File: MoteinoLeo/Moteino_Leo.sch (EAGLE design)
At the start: 21 parts, among them IC3 MCP1703CB, U3 ATMEGA32U4, X1 16Mhz

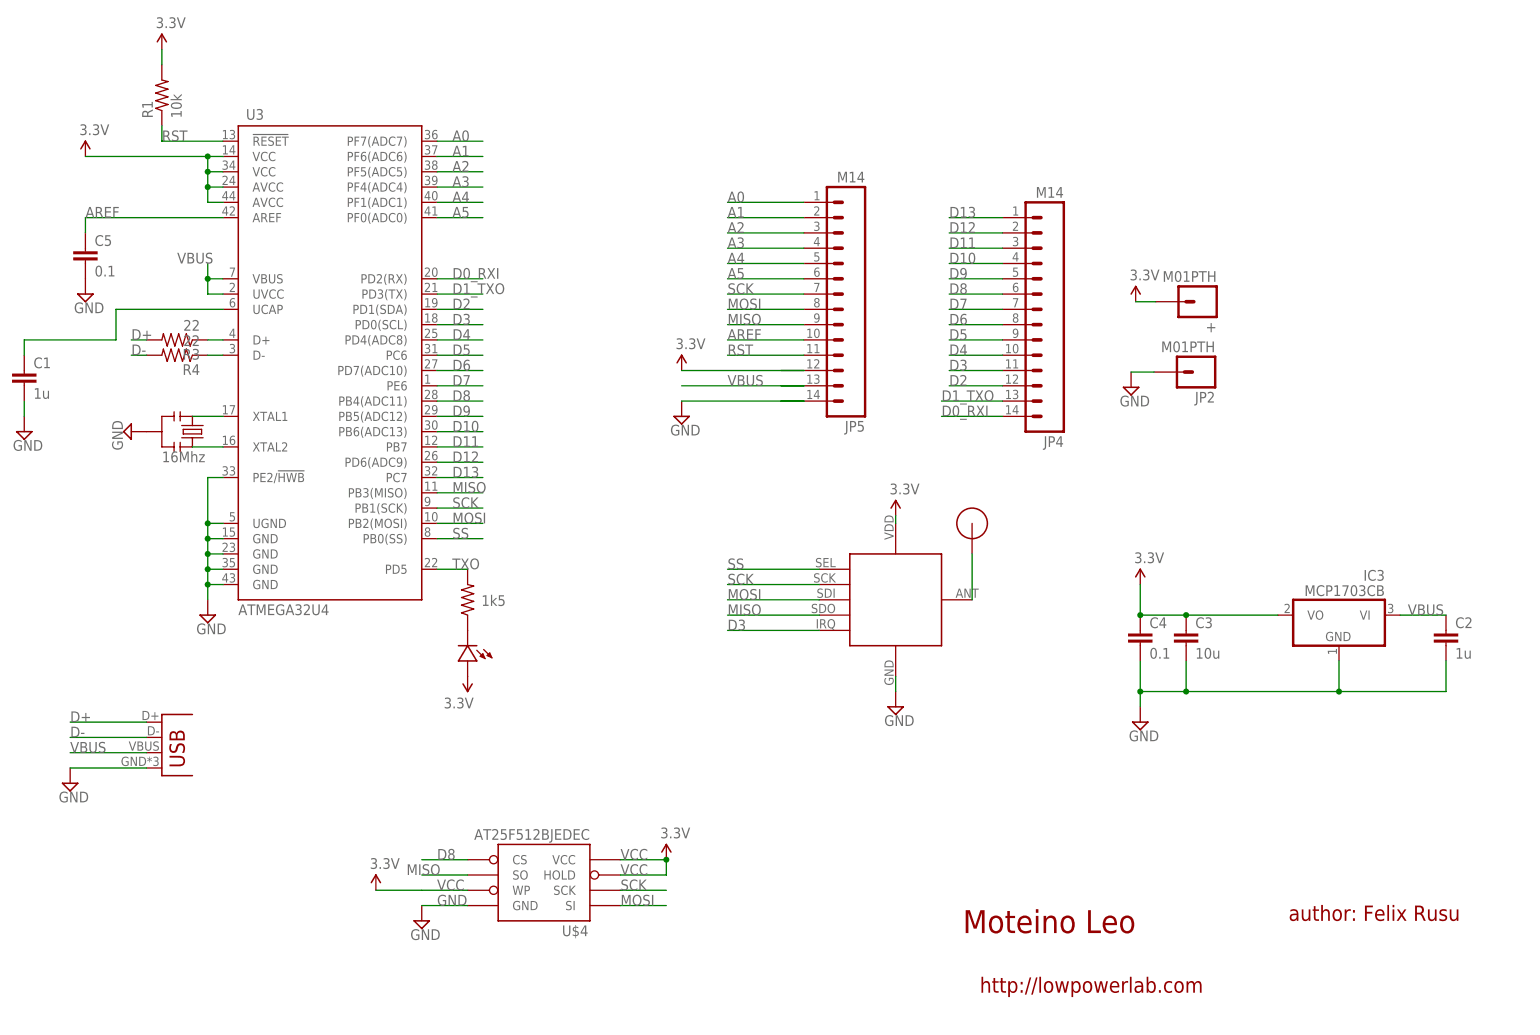
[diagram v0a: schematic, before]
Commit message: Update to R1 production schematic
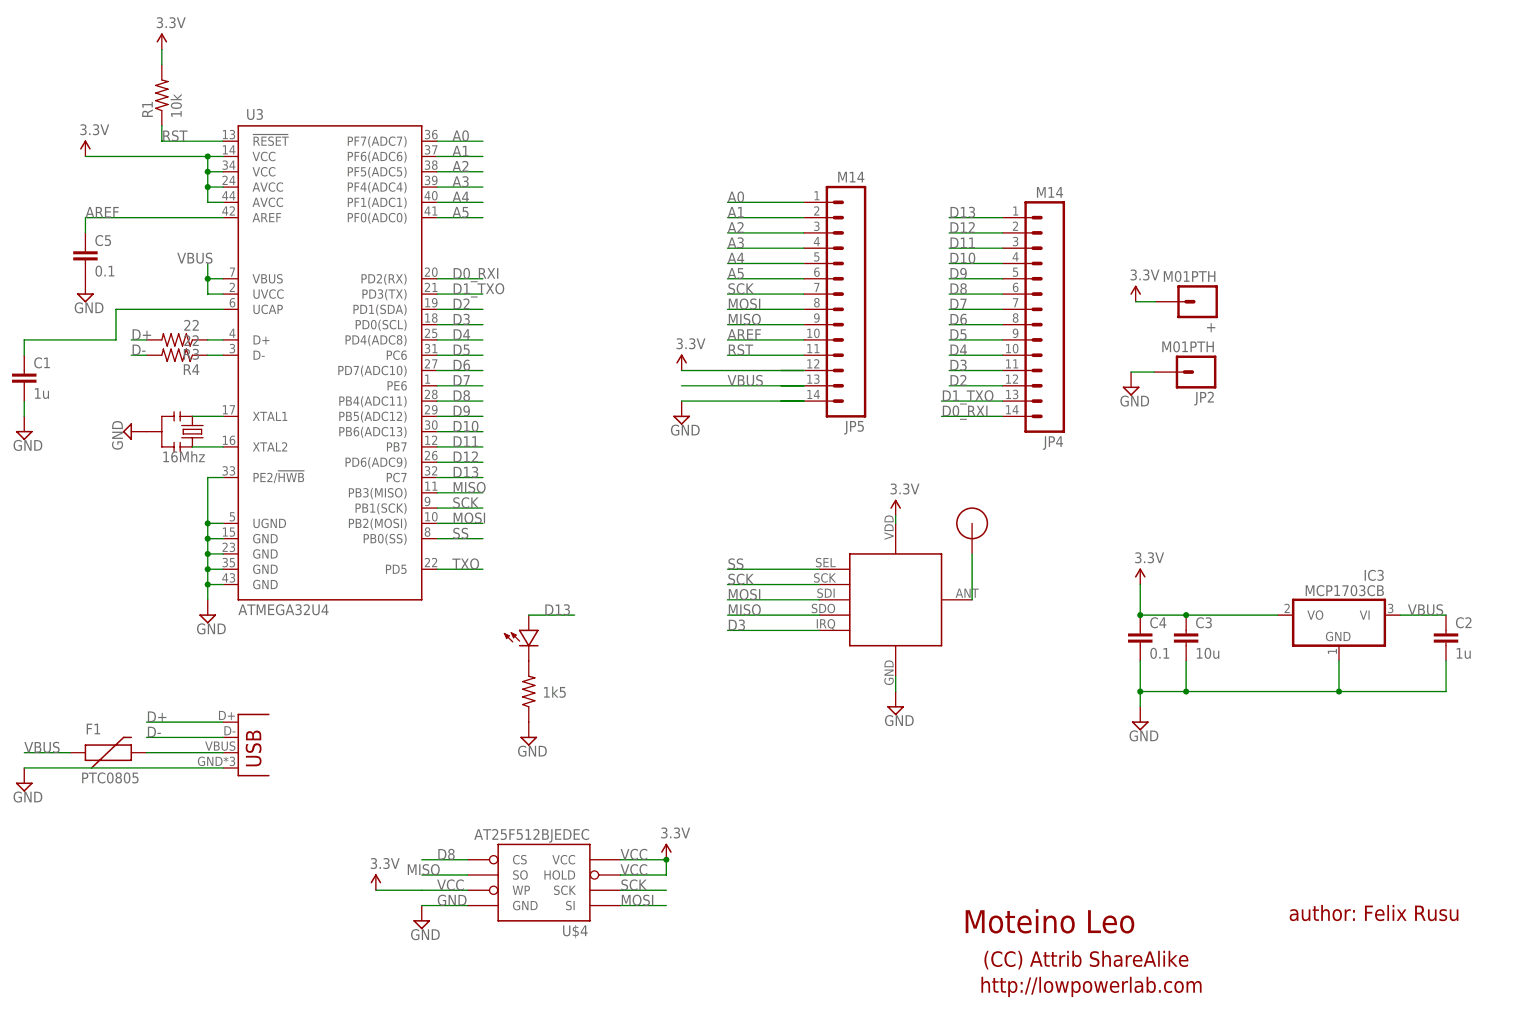
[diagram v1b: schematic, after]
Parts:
- added F1: PTC0805, LowPowerLab:PTC0805
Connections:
- new net USBPOWER: F1.2, JP3.VBUS
- net D13: now also U$2.PLUS
- net GND: now also R2.1
- net N$1: now also R2.2; no longer R2.1
- net TXO: no longer R2.2
- net VBUS: now also F1.1; no longer JP3.VBUS
- net VCC: no longer U$2.PLUS
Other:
- note added: "(CC) Attrib ShareAlike"
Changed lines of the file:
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@@
 <part name="R3" library="LowPowerLab" deviceset="RESISTOR" device="0603-RES" value="22"/>
 <part name="R4" library="LowPowerLab" deviceset="RESISTOR" device="0603-RES" value="22"/>
-<part name="P+6" library="SparkFun" deviceset="VCC" device="" value="3.3V"/>
+<part name="SUPPLY6" library="supply2" deviceset="GND" device=""/>
+<part name="F1" library="LowPowerLab" deviceset="PTC" device="0805"/>
 </parts>
 <sheets>
@@
 <text x="217.678" y="20.32" size="2.54" layer="94" font="vector">author: Felix Rusu</text>
 <text x="166.37" y="8.382" size="2.54" layer="94" font="vector">http://lowpowerlab.com</text>
+<text x="166.878" y="12.7" size="2.54" layer="94" font="vector">(CC) Attrib ShareAlike</text>
 </plain>
 <instances>
@@
 <instance part="C2" gate="G$1" x="243.84" y="66.04"/>
 <instance part="C3" gate="G$1" x="200.66" y="66.04"/>
-<instance part="U$2" gate="G$1" x="81.28" y="66.04" smashed="yes" rot="R270"/>
-<instance part="R2" gate="G$1" x="81.28" y="73.66" smashed="yes" rot="R90">
-<attribute name="VALUE" x="87.63" y="74.422" size="1.778" layer="96" rot="R180"/>
+<instance part="U$2" gate="G$1" x="91.44" y="66.04" smashed="yes" rot="R90"/>
+<instance part="R2" gate="G$1" x="91.44" y="58.42" smashed="yes" rot="R90">
+<attribute name="VALUE" x="97.79" y="59.182" size="1.778" layer="96" rot="R180"/>
 </instance>
 <instance part="RFM12B" gate="G$1" x="152.4" y="73.66" smashed="yes"/>
@@
 <instance part="SUPPLY5" gate="GND" x="7.62" y="101.6"/>
 <instance part="SUPPLY12" gate="GND" x="17.78" y="124.46"/>
-<instance part="JP3" gate="G$1" x="30.48" y="45.72"/>
-<instance part="SUPPLY13" gate="GND" x="15.24" y="43.18"/>
+<instance part="JP3" gate="G$1" x="43.18" y="45.72"/>
+<instance part="SUPPLY13" gate="GND" x="7.62" y="43.18"/>
 <instance part="JP4" gate="G$1" x="180.34" y="119.38" rot="R180"/>
 <instance part="JP5" gate="G$1" x="147.32" y="121.92" rot="R180"/>
 <instance part="R3" gate="G$1" x="33.02" y="116.84" rot="R180"/>
 <instance part="R4" gate="G$1" x="33.02" y="114.3" rot="R180"/>
-<instance part="P+6" gate="1" x="81.28" y="60.96" rot="R180"/>
+<instance part="SUPPLY6" gate="GND" x="91.44" y="50.8"/>
+<instance part="F1" gate="G$1" x="20.32" y="48.26"/>
 </instances>
 <busses>
@@
 <segment>
 <pinref part="JP3" gate="G$1" pin="GND"/>
-<wire x1="27.94" y1="45.72" x2="15.24" y2="45.72" width="0.1524" layer="91"/>
+<wire x1="40.64" y1="45.72" x2="7.62" y2="45.72" width="0.1524" layer="91"/>
 <pinref part="SUPPLY13" gate="GND" pin="GND"/>
+</segment>
+<segment>
+<pinref part="R2" gate="G$1" pin="1"/>
+<pinref part="SUPPLY6" gate="GND" pin="GND"/>
 </segment>
 </net>
@@
 <pinref part="SUPPLY11" gate="1" pin="VCC"/>
 </segment>
-<segment>
-<pinref part="P+6" gate="1" pin="VCC"/>
-<pinref part="U$2" gate="G$1" pin="PLUS"/>
-</segment>
 </net>
 <net name="D9" class="0">
@@
 </segment>
 <segment>
-<pinref part="JP3" gate="G$1" pin="VBUS"/>
-<wire x1="27.94" y1="48.26" x2="15.24" y2="48.26" width="0.1524" layer="91"/>
-<label x="15.24" y="48.26" size="1.778" layer="95"/>
-</segment>
-<segment>
 <wire x1="133.35" y1="109.22" x2="137.16" y2="109.22" width="0.1524" layer="91"/>
 <label x="124.46" y="109.22" size="1.778" layer="95"/>
@@
 <wire x1="137.16" y1="109.22" x2="116.84" y2="109.22" width="0.1524" layer="91"/>
 </segment>
+<segment>
+<pinref part="F1" gate="G$1" pin="1"/>
+<wire x1="15.24" y1="48.26" x2="7.62" y2="48.26" width="0.1524" layer="91"/>
+<label x="7.62" y="48.26" size="1.778" layer="95"/>
+</segment>
 </net>
 <net name="D+" class="0">
@@
 <segment>
 <pinref part="JP3" gate="G$1" pin="D+"/>
-<wire x1="27.94" y1="53.34" x2="15.24" y2="53.34" width="0.1524" layer="91"/>
-<label x="15.24" y="53.34" size="1.778" layer="95"/>
+<wire x1="40.64" y1="53.34" x2="27.94" y2="53.34" width="0.1524" layer="91"/>
+<label x="27.94" y="53.34" size="1.778" layer="95"/>
 </segment>
 </net>
@@
 <segment>
 <pinref part="JP3" gate="G$1" pin="D-"/>
-<wire x1="27.94" y1="50.8" x2="15.24" y2="50.8" width="0.1524" layer="91"/>
-<label x="15.24" y="50.8" size="1.778" layer="95"/>
+<wire x1="40.64" y1="50.8" x2="27.94" y2="50.8" width="0.1524" layer="91"/>
+<label x="27.94" y="50.8" size="1.778" layer="95"/>
 </segment>
 </net>
@@
 <pinref part="JP4" gate="G$1" pin="1"/>
 </segment>
+<segment>
+<pinref part="U$2" gate="G$1" pin="PLUS"/>
+<wire x1="91.44" y1="71.12" x2="99.06" y2="71.12" width="0.1524" layer="91"/>
+<label x="93.98" y="71.12" size="1.778" layer="95"/>
+</segment>
 </net>
 <net name="N$7" class="0">
@@
 <segment>
 <pinref part="U3" gate="G$1" pin="PD5"/>
-<pinref part="R2" gate="G$1" pin="2"/>
-<wire x1="76.2" y1="78.74" x2="81.28" y2="78.74" width="0.1524" layer="91"/>
+<wire x1="76.2" y1="78.74" x2="83.82" y2="78.74" width="0.1524" layer="91"/>
 <label x="78.74" y="78.74" size="1.778" layer="95"/>
 </segment>
@@
 <net name="N$1" class="0">
 <segment>
-<pinref part="R2" gate="G$1" pin="1"/>
+<pinref part="R2" gate="G$1" pin="2"/>
 <pinref part="U$2" gate="G$1" pin="MINUS"/>
 </segment>
 </net>
+<net name="USBPOWER" class="1">
+<segment>
+<pinref part="JP3" gate="G$1" pin="VBUS"/>
+<wire x1="40.64" y1="48.26" x2="27.94" y2="48.26" width="0.1524" layer="91"/>
+<pinref part="F1" gate="G$1" pin="2"/>
+</segment>
+</net>

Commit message: Update Moteino_Leo.sch
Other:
- note added: "http://www.moteino.com"
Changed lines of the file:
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@@
 <setting verticaltext="up"/>
 </settings>
-<grid distance="0.1" unitdist="inch" unit="inch" style="lines" multiple="1" display="no" altdistance="0.01" altunitdist="inch" altunit="inch"/>
+<grid distance="0.01" unitdist="inch" unit="inch" style="lines" multiple="1" display="no" altdistance="0.01" altunitdist="inch" altunit="inch"/>
 <layers>
 <layer number="1" name="Top" color="4" fill="1" visible="no" active="no"/>
@@
 <text x="166.37" y="8.382" size="2.54" layer="94" font="vector">http://lowpowerlab.com</text>
 <text x="166.878" y="12.7" size="2.54" layer="94" font="vector">(CC) Attrib ShareAlike</text>
+<text x="166.37" y="4.826" size="2.54" layer="94" font="vector">http://www.moteino.com</text>
 </plain>
 <instances>
